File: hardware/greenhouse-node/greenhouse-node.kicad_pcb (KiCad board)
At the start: 2 copper layers, 90.2 x 69.8 mm, 51 parts, among them J1 Conn_01x12_Male, J2 Conn_01x02_Male, J3 Conn_01x02_Male, J4 Conn_01x02_Male, J5 Conn_01x04_Male, J6 RX_PinHeader_1x04_P2.54mm, J7 TX_PinHeader_1x04_P2.54mm, J8 Conn_01x02_Male, Q1 BC549C, Q2 BC549C, Q3 BC549C, Q4 IRF9530N, Q5 IRF530N, Q6 IRF9530N, Q7 IRF530N, Q8 BC549C, Q9 BC549C, U1 ATtiny84A-P, U2 L7805, U3 74HC595

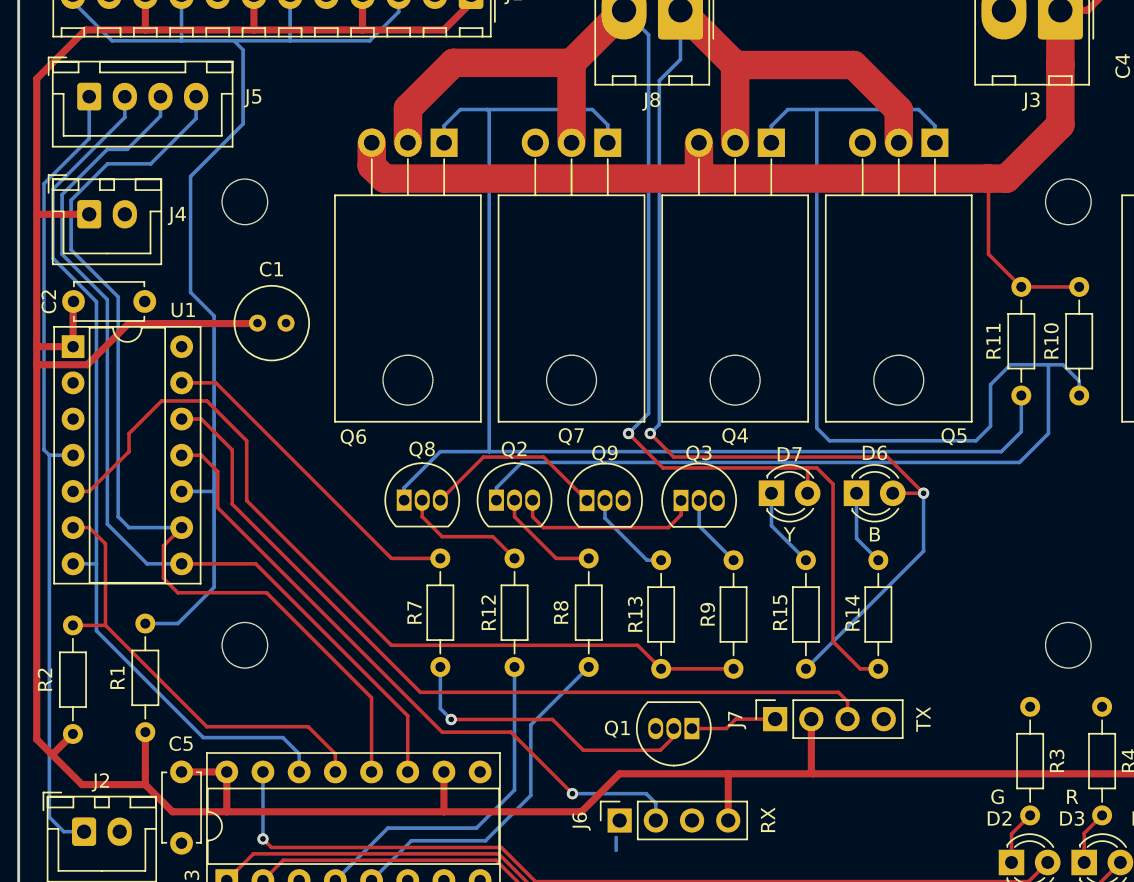
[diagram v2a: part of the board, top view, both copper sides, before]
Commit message: Add crystal to node board
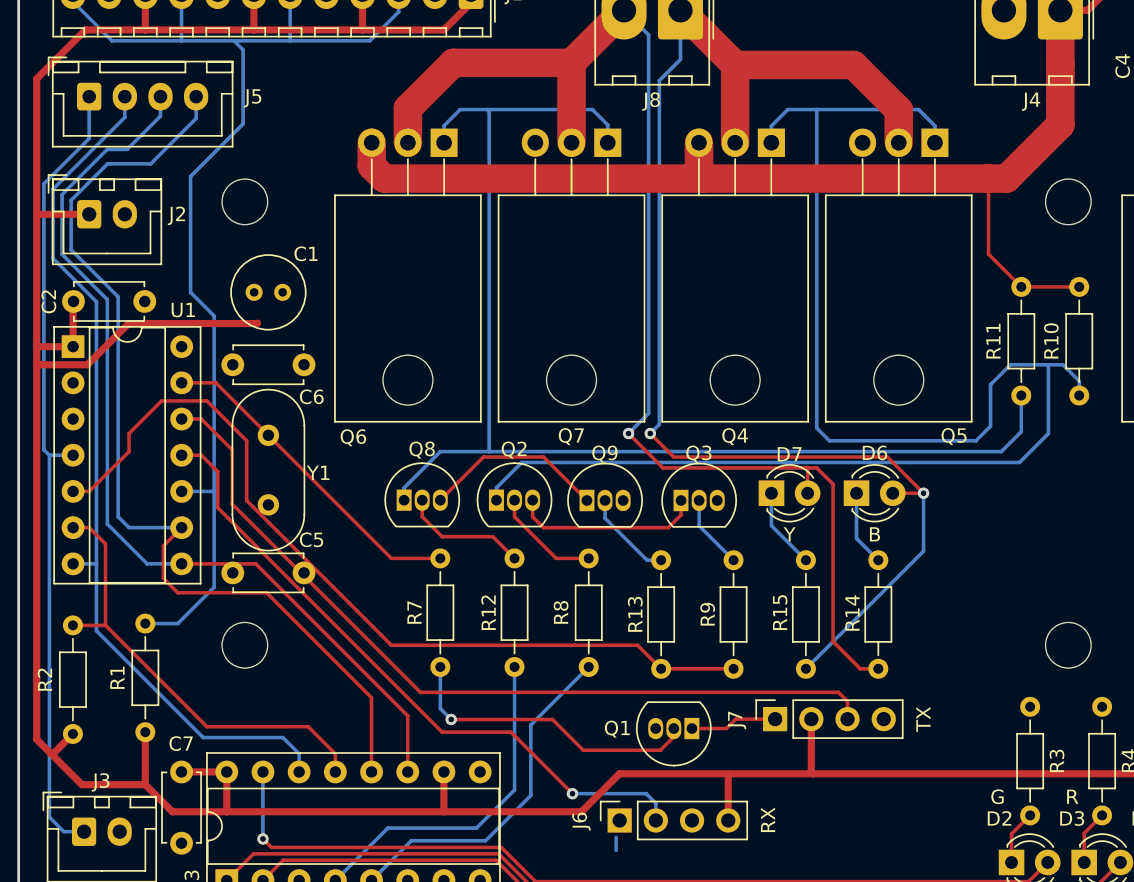
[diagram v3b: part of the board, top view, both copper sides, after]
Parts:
- added C5: 22pF, Capacitor_THT:C_Disc_D4.7mm_W2.5mm_P5.00mm, F.Cu at (143.3, 91.4)
- added C6: 22pF, Capacitor_THT:C_Disc_D4.7mm_W2.5mm_P5.00mm, F.Cu at (143.3, 76.8)
- added Y1: Crystal_Small, Crystal:Crystal_HC49-U_Vertical, F.Cu at (145.8, 81.8)
- moved C1 2.17 mm to (144.8, 71.8)
- renumbered C5 to C7, J4 to J2, J2 to J3, J3 to J4
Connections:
- U1 pad 2: unconnected-(U1-Pad2) -> /XTAL1
- U1 pad 3: unconnected-(U1-Pad3) -> /XTAL2

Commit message: Add value to PCB
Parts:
- Y1: value Crystal_Small -> 8MHz
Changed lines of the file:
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@@
       (effects (font (size 1 1) (thickness 0.15)))
     )
-    (fp_text value "Crystal_Small" (at 2.44 3.525 90) (layer "F.Fab")
-      (effects (font (size 1 1) (thickness 0.15)))
-    )
-    (fp_text user "${REFERENCE}" (at 2.44 0 90) (layer "F.Fab")
+    (fp_text value "8MHz" (at 2.921 0 180) (layer "F.Fab")
+      (effects (font (size 1 1) (thickness 0.15)))
+    )
+    (fp_text user "${REFERENCE}" (at 1.651 0 180) (layer "F.Fab")
       (effects (font (size 1 1) (thickness 0.15)))
     )
@@
       (effects (font (size 1 1) (thickness 0.15)))
     )
-    (fp_text value "22pF" (at 2.5 2.5) (layer "F.Fab")
+    (fp_text value "22pF" (at 2.627 1.25) (layer "F.Fab")
       (effects (font (size 1 1) (thickness 0.15)))
     )
@@
       (effects (font (size 1 1) (thickness 0.15)))
     )
-    (fp_text value "100uF" (at 1 3.75) (layer "F.Fab")
+    (fp_text value "100uF" (at 1.127 -1.27) (layer "F.Fab")
       (effects (font (size 1 1) (thickness 0.15)))
     )
@@
       (effects (font (size 1 1) (thickness 0.15)))
     )
-    (fp_text value "22pF" (at 2.5 2.5) (layer "F.Fab")
-      (effects (font (size 1 1) (thickness 0.15)))
-    )
+    (fp_text value "22pF" (at 2.627 1.27) (layer "F.Fab")
+      (effects (font (size 1 1) (thickness 0.15)))
+    )

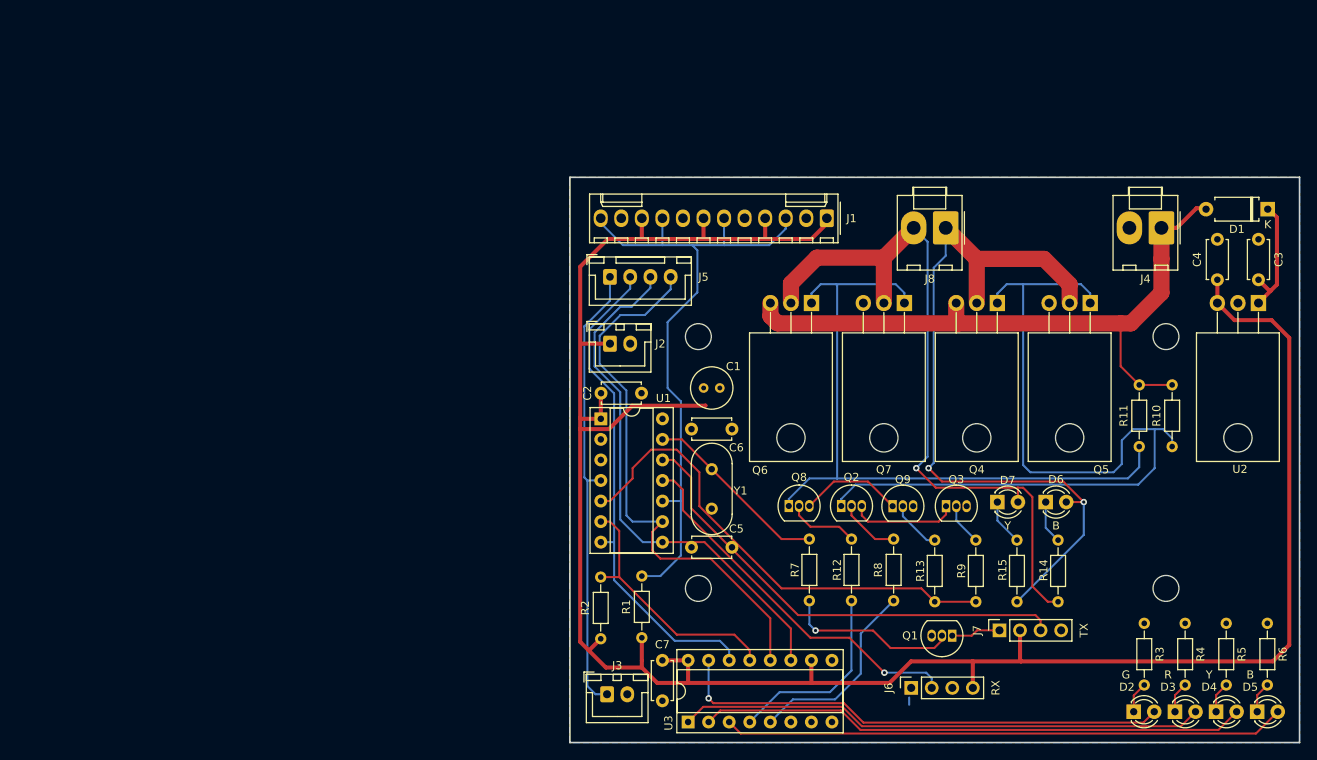
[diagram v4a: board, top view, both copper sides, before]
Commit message: Repositioned DIPs
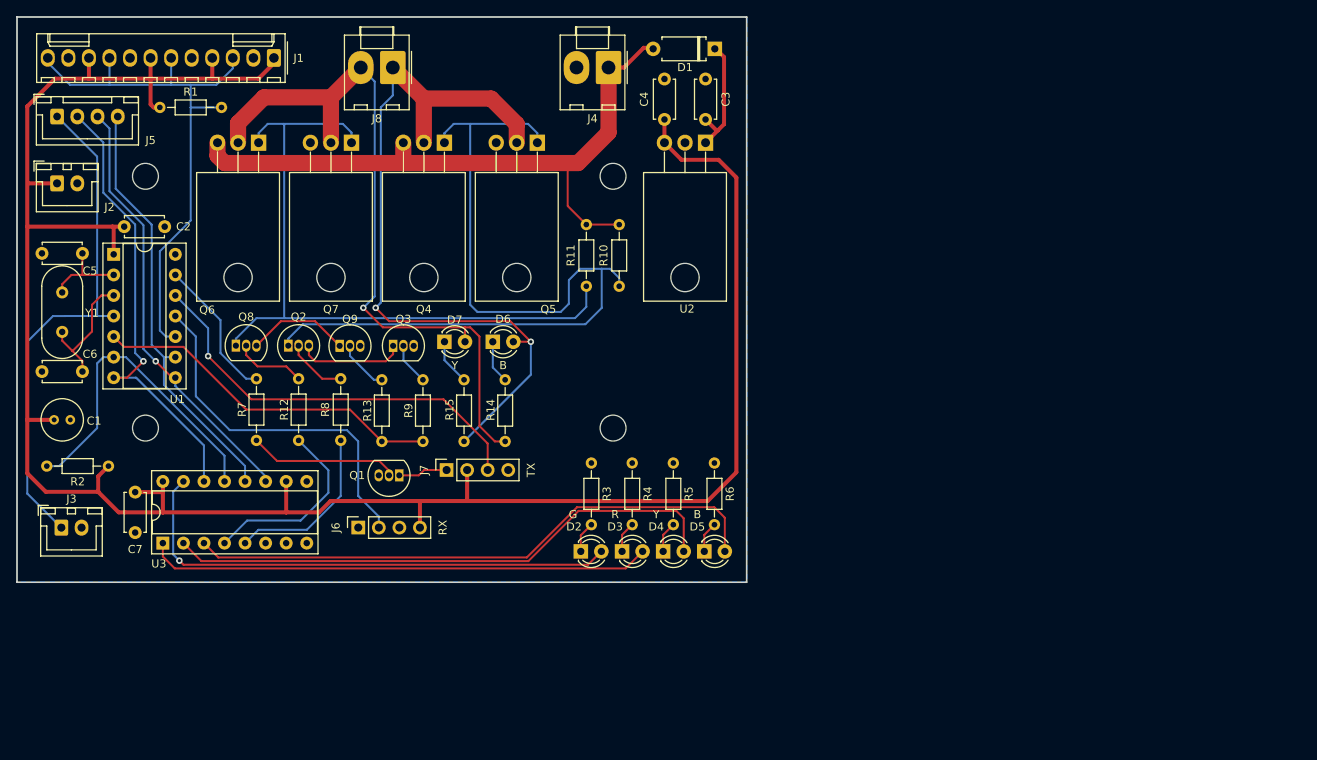
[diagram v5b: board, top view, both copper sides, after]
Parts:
- D1: value D -> 1N5408RL
- Y1: footprint Crystal:Crystal_HC49-U_Vertical -> Crystal:Crystal_HC49-4H_Vertical
- moved R1 88.6 mm to (77.6, 37.1), turned to 0 degrees
- moved C5 83.6 mm to (68.0, 55.1), turned to 180 degrees
- moved Y1 83.2 mm to (65.5, 59.9)
- moved C1 80.4 mm to (64.5, 75.7)
- moved C6 75.6 mm to (68.0, 69.7), turned to 180 degrees
- moved C3 71.1 mm to (145.0, 33.6)
- moved R3 71.1 mm to (130.9, 81.0)
- moved R6 71.1 mm to (146.1, 81.0)
- moved U2 71.1 mm to (145.0, 41.4)
- moved D6 71.1 mm to (118.7, 66.0)
- moved D7 71.1 mm to (112.8, 66.0)
- moved H3 71.1 mm to (75.8, 45.6)
- moved H4 71.1 mm to (75.8, 76.7)
- moved J1 71.1 mm to (91.7, 31.0)
- moved J2 71.1 mm to (64.9, 46.5)
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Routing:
- net Motor_PWM: track 60.0 -> 43.6 mm
- net /XTAL2: track 0.00 -> 15.8 mm
- net /SR_RCLK: track 68.4 -> 53.2 mm
- net /SR_CLK: track 65.6 -> 53.9 mm, vias 0 -> 1
- net /OneWire: track 81.8 -> 70.7 mm
- net /XTAL1: track 0.00 -> 10.5 mm
- net /SR_OE: track 31.9 -> 40.4 mm
- net /RAD_TX: track 58.4 -> 51.5 mm, vias 0 -> 1
- net /Reset: track 56.6 -> 63.4 mm
- net /RAD_TX_EN: track 23.3 -> 17.7 mm
- net /SR_SER: track 61.5 -> 57.2 mm, vias 0 -> 1
- net Motor_A: track 24.3 -> 21.1 mm
- net Net-(Q1-Pad2): track 21.5 -> 18.5 mm, vias 1 -> 0
- net /LED_B: track 69.5 -> 72.4 mm
- net /LED_R: track 65.2 -> 62.4 mm
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
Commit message: Tweaking traces
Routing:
- net /Reset: track 63.4 -> 56.7 mm
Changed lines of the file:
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@@
   (segment (start 102.108 85.09) (end 104.658 87.64) (width 0.25) (layer "B.Cu") (net 3))
   (segment (start 102.108 78.359) (end 102.108 85.09) (width 0.25) (layer "B.Cu") (net 3))
-  (segment (start 85.09 67.437) (end 88.265 70.612) (width 0.25) (layer "B.Cu") (net 4))
-  (segment (start 85.09 63.358) (end 85.09 67.437) (width 0.25) (layer "B.Cu") (net 4))
-  (segment (start 79.512 57.78) (end 85.09 63.358) (width 0.25) (layer "B.Cu") (net 4))
+  (segment (start 79.512 57.78) (end 84.074 62.342) (width 0.25) (layer "B.Cu") (net 4))
   (segment (start 88.265 70.612) (end 89.535 70.612) (width 0.25) (layer "B.Cu") (net 4))
+  (segment (start 84.074 62.342) (end 84.074 66.421) (width 0.25) (layer "B.Cu") (net 4))
+  (segment (start 84.074 66.421) (end 88.265 70.612) (width 0.25) (layer "B.Cu") (net 4))
   (segment (start 89.535 63.119) (end 92.964 63.119) (width 0.25) (layer "B.Cu") (net 5))
   (segment (start 86.995 66.527) (end 86.995 65.659) (width 0.25) (layer "B.Cu") (net 5))
@@
   (segment (start 79.512 71.511) (end 79.512 70.48) (width 0.25) (layer "B.Cu") (net 13))
   (segment (start 71.374 39.687) (end 69.897 38.21) (width 0.25) (layer "B.Cu") (net 13))
+  (segment (start 71.892 67.94) (end 70.231 69.601) (width 0.25) (layer "F.Cu") (net 14))
+  (segment (start 70.231 78.232) (end 67.056 81.407) (width 0.25) (layer "F.Cu") (net 14))
+  (segment (start 70.231 69.601) (end 70.231 78.232) (width 0.25) (layer "F.Cu") (net 14))
+  (segment (start 67.056 81.407) (end 63.627 81.407) (width 0.25) (layer "F.Cu") (net 14))
   (segment (start 85.588 83.302) (end 85.588 80.127) (width 0.25) (layer "B.Cu") (net 14))
-  (segment (start 69.85 76.708) (end 65.151 81.407) (width 0.25) (layer "B.Cu") (net 14))
   (segment (start 73.401 67.94) (end 71.892 67.94) (width 0.25) (layer "B.Cu") (net 14))
   (segment (start 85.588 80.127) (end 73.401 67.94) (width 0.25) (layer "B.Cu") (net 14))
-  (segment (start 70.617 67.94) (end 69.85 68.707) (width 0.25) (layer "B.Cu") (net 14))
-  (segment (start 69.85 68.707) (end 69.85 76.708) (width 0.25) (layer "B.Cu") (net 14))
-  (segment (start 65.151 81.407) (end 63.627 81.407) (width 0.25) (layer "B.Cu") (net 14))
-  (segment (start 71.892 67.94) (end 70.617 67.94) (width 0.25) (layer "B.Cu") (net 14))
   (segment (start 85.217 37.084) (end 81.407 37.084) (width 0.25) (layer "B.Cu") (net 15))
   (segment (start 71.374 30.968) (end 71.374 34.29) (width 0.25) (layer "B.Cu") (net 15))
@@
   (segment (start 78.354 65.4) (end 77.597 64.643) (width 0.25) (layer "B.Cu") (net 15))
   (segment (start 77.597 64.643) (end 77.597 54.864) (width 0.25) (layer "B.Cu") (net 15))
+  (segment (start 83.058 67.437) (end 83.185 67.437) (width 0.25) (layer "F.Cu") (net 16))
+  (segment (start 83.185 67.437) (end 88.9 73.152) (width 0.25) (layer "F.Cu") (net 16))
+  (segment (start 112.649 73.152) (end 118.11 78.613) (width 0.25) (layer "F.Cu") (net 16))
+  (segment (start 88.9 73.152) (end 112.649 73.152) (width 0.25) (layer "F.Cu") (net 16))
   (segment (start 118.11 78.613) (end 118.11 81.89) (width 0.25) (layer "F.Cu") (net 16))
-  (segment (start 112.649 73.152) (end 118.11 78.613) (width 0.25) (layer "F.Cu") (net 16))
-  (segment (start 83.566 67.818) (end 88.9 73.152) (width 0.25) (layer "F.Cu") (net 16))
-  (segment (start 88.9 73.152) (end 112.649 73.152) (width 0.25) (layer "F.Cu") (net 16))
-  (via (at 83.566 67.818) (size 0.8) (drill 0.4) (layers "F.Cu" "B.Cu") (net 16))
-  (segment (start 83.566 64.374) (end 83.566 67.818) (width 0.25) (layer "B.Cu") (net 16))
-  (segment (start 79.512 60.32) (end 83.566 64.374) (width 0.25) (layer "B.Cu") (net 16))
+  (via (at 83.058 67.437) (size 0.8) (drill 0.4) (layers "F.Cu" "B.Cu") (net 16))
+  (segment (start 83.058 67.437) (end 83.058 63.866) (width 0.25) (layer "B.Cu") (net 16))
+  (segment (start 83.058 63.866) (end 79.512 60.32) (width 0.25) (layer "B.Cu") (net 16))
   (segment (start 80.01 93.091) (end 80.518 93.599) (width 0.25) (layer "F.Cu") (net 17))
   (segment (start 80.518 93.599) (end 130.5056 93.599) (width 0.25) (layer "F.Cu") (net 17))
@@
   (segment (start 105.918 82.55) (end 105.918 81.968654) (width 0.25) (layer "F.Cu") (net 34))
   (segment (start 105.918 81.968654) (end 104.721346 80.772) (width 0.25) (layer "F.Cu") (net 34))
-  (segment (start 61.214 66.04) (end 61.214 84.799) (width 0.25) (layer "B.Cu") (net 35))
   (segment (start 69.85 62.855) (end 69.845 62.86) (width 0.25) (layer "B.Cu") (net 35))
   (segment (start 69.85 43.163) (end 69.85 62.855) (width 0.25) (layer "B.Cu") (net 35))
   (segment (start 64.897 38.21) (end 69.85 43.163) (width 0.25) (layer "B.Cu") (net 35))
-  (segment (start 69.845 62.86) (end 65.97572 62.86) (width 0.25) (layer "B.Cu") (net 35))
-  (segment (start 65.97572 62.86) (end 65.97072 62.865) (width 0.25) (layer "B.Cu") (net 35))
-  (segment (start 65.97072 62.865) (end 64.389 62.865) (width 0.25) (layer "B.Cu") (net 35))
-  (segment (start 64.389 62.865) (end 61.214 66.04) (width 0.25) (layer "B.Cu") (net 35))
-  (segment (start 61.214 84.799) (end 65.425 89.01) (width 0.25) (layer "B.Cu") (net 35))
+  (segment (start 65.405 88.99) (end 65.425 89.01) (width 0.25) (layer "B.Cu") (net 35))
+  (segment (start 65.405 82.423) (end 65.405 88.99) (width 0.25) (layer "B.Cu") (net 35))
+  (segment (start 69.845 77.983) (end 65.405 82.423) (width 0.25) (layer "B.Cu") (net 35))
   (segment (start 71.892 62.86) (end 69.845 62.86) (width 0.25) (layer "B.Cu") (net 35))
+  (segment (start 69.845 62.86) (end 69.845 77.983) (width 0.25) (layer "B.Cu") (net 35))
   (segment (start 107.696 68.326) (end 110.109 70.739) (width 0.25) (layer "B.Cu") (net 36))
   (segment (start 107.696 66.548) (end 107.696 68.326) (width 0.25) (layer "B.Cu") (net 36))
